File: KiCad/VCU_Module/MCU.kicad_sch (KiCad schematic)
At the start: 0 parts

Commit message: added peripheral pins with the most functionality based on stm32c092rc datasheet, started placing components and routing traces on pcb
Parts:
- added C13, C15, C16, C17: 100n, Capacitor_SMD:C_0805_2012Metric, symbol Device:C_Small
- added C14: 1u, Capacitor_SMD:C_0805_2012Metric, symbol Device:C_Small
- added CR2: ESDCAN03-2BWY, VMS_Footprints:SOT323-3L_STM, symbol ESDCAN03-2BWY:ESDCAN03-2BWY
- added D3: LED, LED_SMD:LED_0805_2012Metric_Pad1.15x1.40mm_HandSolder, symbol Device:LED
- added IC1: STM32C092RCT6, VMS_Footprints:QFP50P1200X1200X160-64N, symbol STM32C092RCT6:STM32C092RCT6
- added J11: Conn_ST_STDC14, Connector_PinHeader_1.27mm:PinHeader_2x07_P1.27mm_Vertical, symbol Connector:Conn_ST_STDC14
- added R24, R25: 10k, Resistor_SMD:R_0805_2012Metric, symbol Device:R_Small_US
- added R26: 120, Resistor_SMD:R_0805_2012Metric, symbol Device:R_Small_US
- added R27, R28: 1k, Resistor_SMD:R_0805_2012Metric, symbol Device:R_Small_US
- added SW2: SW_Push, Button_Switch_THT:SW_PUSH_6mm_H4.3mm, symbol Switch:SW_Push
- added TP12, TP13, TP14, TP15, TP16: TestPoint_Small, TestPoint:TestPoint_THTPad_D1.5mm_Drill0.7mm, symbol Connector:TestPoint_Square
- added U6: MCP2562FDT-H_SN, VMS_Footprints:SOIC127P600X175-8N, symbol MCP2562FDT-H_SN:MCP2562FDT-H_SN
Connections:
- new net: C13.2, IC1.12 (PF2-NRST), J11.12 (~{RST}), R24.2, SW2.1
- new net: D3.2 (A), R27.2
- new net: IC1.30 (PB10), R27.1, R28.1
- new net: IC1.19 (PA2), J11.13 (VCP_RX)
- new net: IC1.20 (PA3), J11.14 (VCP_TX)
- new net: IC1.45 (PA13), J11.4 (JTMS/SWDIO)
- new net: IC1.46 (PA14-BOOT0), J11.6 (JCLK/SWCLK)
- new net +3V3: C14.1, C15.1, C17.1, IC1.7 (VREF+), IC1.8 (VDD/VDDA), J11.3 (VCC), R24.1, U6.5 (VIO)
- new net +5V: C16.2, U6.3 (VDD)
- new net ADC0: IC1.17 (PA0)
- new net ADC1: IC1.18 (PA1)
- new net ADC4: IC1.21 (PA4)
- new net ADC8: IC1.36 (PA8)
- new net CANH: CR2.1, R26.2, TP16.1, U6.7 (CANH)
- new net CANL: CR2.2, R26.1, TP15.1, U6.6 (CANL)
- new net CAN_RXD: IC1.50 (PD0), TP13.1, U6.4 (RXD)
- new net CAN_TXD: IC1.51 (PD1), TP12.1, U6.1 (TXD)
- new net FAULT_LED: R28.2
- new net GND: C13.1, C14.2, C15.2, C16.1, C17.2, CR2.3, D3.1 (K), IC1.9 (VSS/VSSA), J11.11 (GNDDetect), J11.5 (GND), J11.7 (GND), R25.2, SW2.2, U6.2 (VSS)
- new net GPIO_SPARE1_PB6: IC1.60 (PB6)
- new net GPIO_SPARE2_PB7: IC1.61 (PB7)
- new net GPIO_SPARE3_PB8: IC1.62 (PB8)
- new net GPIO_SPARE4_PB9: IC1.63 (PB9)
- new net I2C1_SCL: IC1.37 (PA9)
- new net I2C1_SDA: IC1.42 (PA10)
- new net PB3: IC1.57 (PB3), J11.8 (JTDO/SWO)
- new net SPI1_MISO: IC1.23 (PA6)
- new net SPI1_MOSI: IC1.24 (PA7)
- new net SPI1_NSS: IC1.47 (PA15)
- new net SPI1_SCK: IC1.22 (PA5)
- new net STDBY: IC1.52 (PD2), R25.1, TP14.1, U6.8 (STBY)
- new net TIM1_CH1: IC1.48 (PC8)
- new net TIM1_CH2: IC1.49 (PC9)
- new net TIM1_CH4: IC1.1 (PC11)
- new net TIM1_ETR/BKIN: IC1.3 (PC13)
- new net TIM2_CH1: IC1.25 (PC4)
- new net TIM2_CH2: IC1.26 (PC5)
- no-connect marks 0 -> 29
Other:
- note added: "CAN_STBY: MCU output; HIGH = CAN standby, LOW = normal mode"
- note added: "MCU PIN ASSIGNMENT / INTERFACE SUMMARY Function MCU Pin Net Name Direction / Notes --------------------------------------------------------------- SWDIO PA13 SWDIO STDC14 debug / programming SWCLK PA14 SWCLK STDC14 debug / programming NRST PF2 NRST Hardware reset; connected to reset button and STDC14 RST CAN RX PD0 CAN_RX MCU receives from CAN transceiver RXD CAN TX PD1 CAN_TX MCU transmits to CA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"
- note added: "Populate only if BMU is end node"
- company: (none) -> VIKING MOTOR SPORTS (VMS)
- title: (none) -> VEHICLE CONTROL UNIT (VCU) MODULE

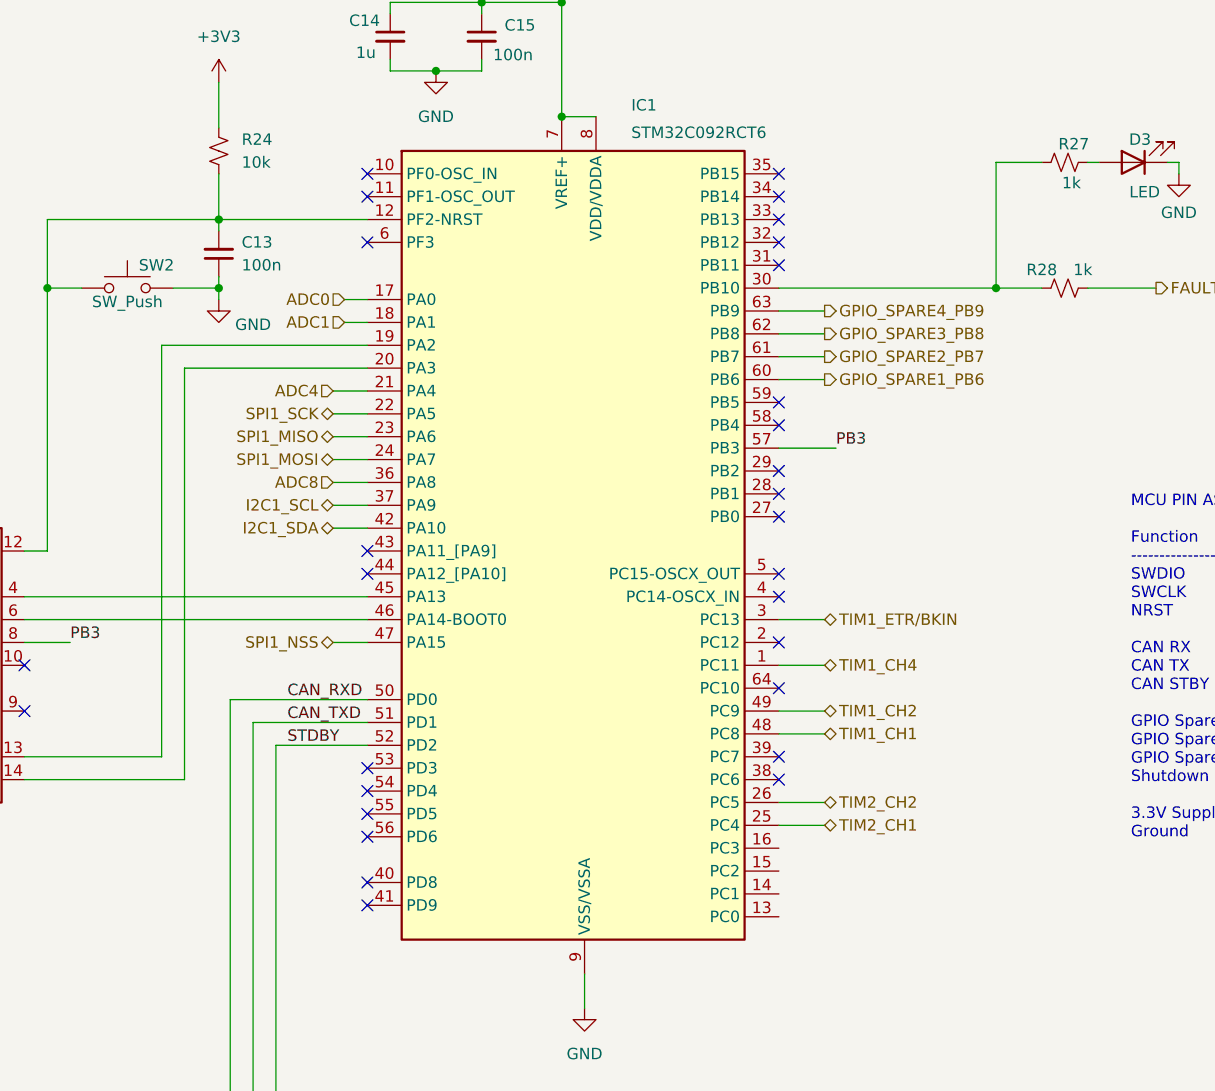
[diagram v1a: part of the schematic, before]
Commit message: adding 'devkit' headers to make connections sustomizable inside of the enclosure
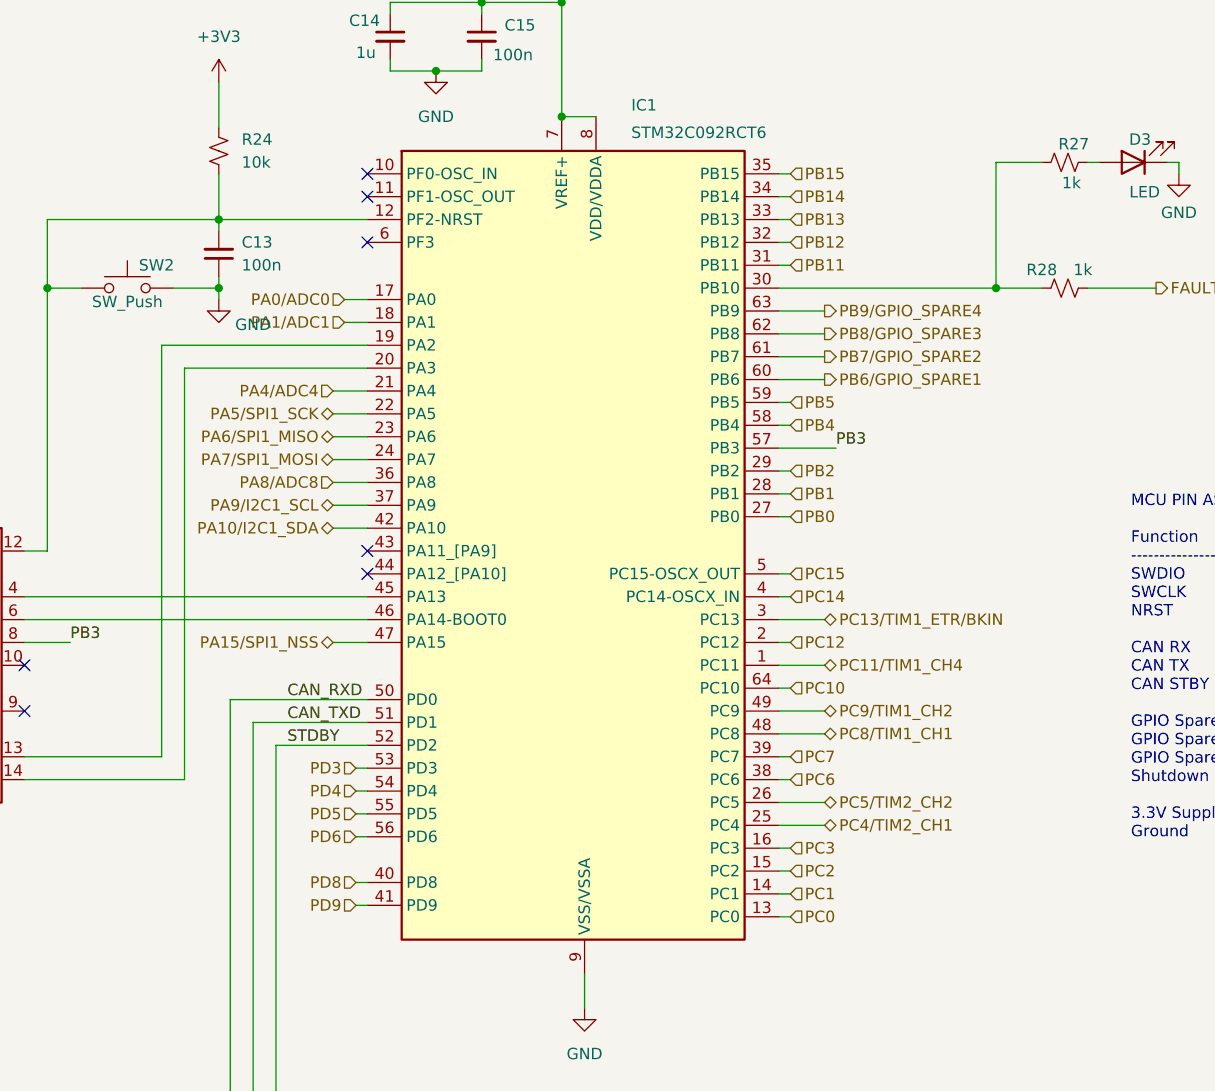
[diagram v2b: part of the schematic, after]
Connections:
- net PC0: now reaches IC1.13 (PC0)
- net PC1: now reaches IC1.14 (PC1)
- net PC2: now reaches IC1.15 (PC2)
- net PC3: now reaches IC1.16 (PC3)
- net PC12: now reaches IC1.2 (PC12)
- net PB0: now reaches IC1.27 (PB0)
- net PB1: now reaches IC1.28 (PB1)
- net PB2: now reaches IC1.29 (PB2)
- net PB11: now reaches IC1.31 (PB11)
- net PB12: now reaches IC1.32 (PB12)
- net PB13: now reaches IC1.33 (PB13)
- net PB14: now reaches IC1.34 (PB14)
- net PB15: now reaches IC1.35 (PB15)
- net PC6: now reaches IC1.38 (PC6)
- net PC7: now reaches IC1.39 (PC7)
- net PC14: now reaches IC1.4 (PC14-OSCX_IN)
- net PD8: now reaches IC1.40 (PD8)
- net PD9: now reaches IC1.41 (PD9)
- net PC15: now reaches IC1.5 (PC15-OSCX_OUT)
- net PD3: now reaches IC1.53 (PD3)
- net PD4: now reaches IC1.54 (PD4)
- net PD5: now reaches IC1.55 (PD5)
- net PD6: now reaches IC1.56 (PD6)
- net PB4: now reaches IC1.58 (PB4)
- net PB5: now reaches IC1.59 (PB5)
- net PC10: now reaches IC1.64 (PC10)
- net ADC0 renamed PA0/ADC0
- net ADC1 renamed PA1/ADC1
- net ADC4 renamed PA4/ADC4
- net ADC8 renamed PA8/ADC8
- net GPIO_SPARE1_PB6 renamed PB6/GPIO_SPARE1
- net GPIO_SPARE2_PB7 renamed PB7/GPIO_SPARE2
- net GPIO_SPARE3_PB8 renamed PB8/GPIO_SPARE3
- net GPIO_SPARE4_PB9 renamed PB9/GPIO_SPARE4
- net I2C1_SCL renamed PA9/I2C1_SCL
- net I2C1_SDA renamed PA10/I2C1_SDA
- net SPI1_MISO renamed PA6/SPI1_MISO
- net SPI1_MOSI renamed PA7/SPI1_MOSI
- net SPI1_NSS renamed PA15/SPI1_NSS
- net SPI1_SCK renamed PA5/SPI1_SCK
- net TIM1_CH1 renamed PC8/TIM1_CH1
- net TIM1_CH2 renamed PC9/TIM1_CH2
- net TIM1_CH4 renamed PC11/TIM1_CH4
- net TIM1_ETR/BKIN renamed PC13/TIM1_ETR/BKIN
- net TIM2_CH1 renamed PC4/TIM2_CH1
- net TIM2_CH2 renamed PC5/TIM2_CH2
- no-connect marks 29 -> 7

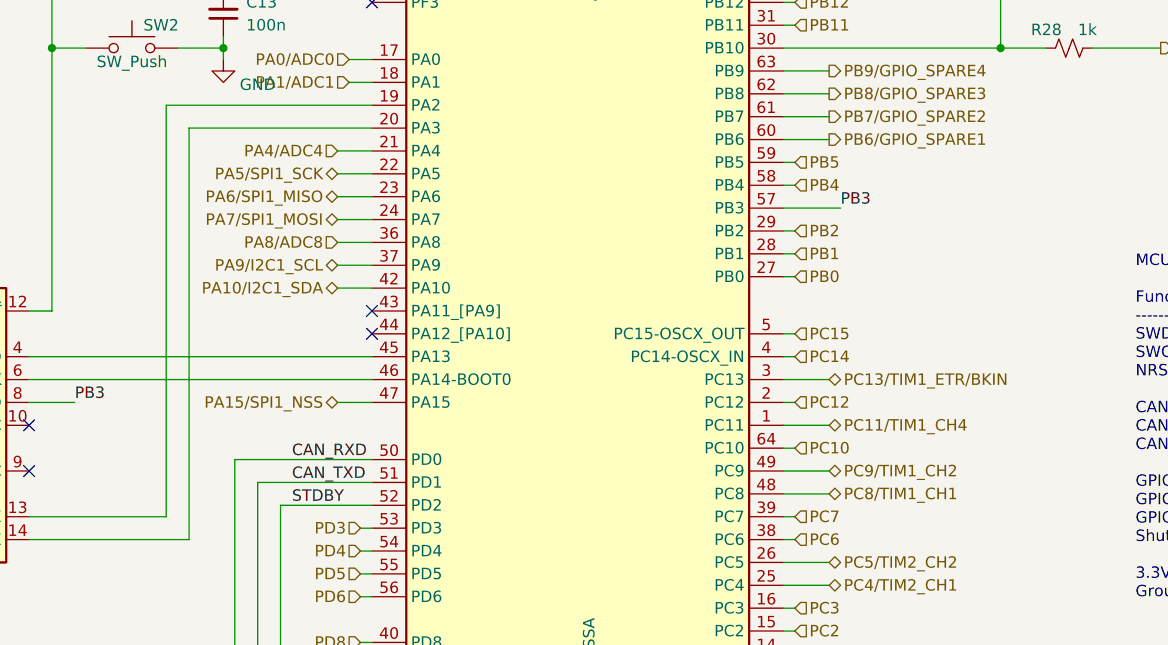
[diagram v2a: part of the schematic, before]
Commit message: added new power supply components, new power supply circuitry needs finishing
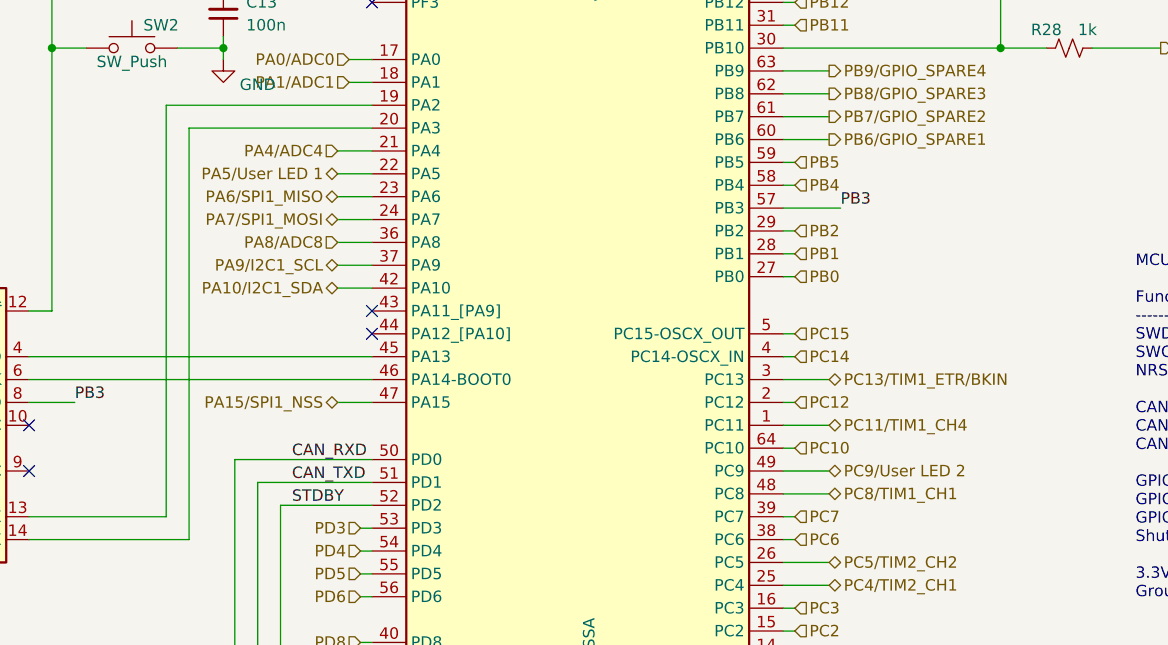
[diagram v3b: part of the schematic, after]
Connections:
- net PA5/SPI1_SCK renamed PA5/User LED 1
- net PC9/TIM1_CH2 renamed PC9/User LED 2
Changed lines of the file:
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@@
 		)
 	)
-	(hierarchical_label "PC9{slash}TIM1_CH2"
+	(hierarchical_label "PC9{slash}User LED 2"
 		(shape bidirectional)
 		(at 212.09 128.27 0)
@@
 		)
 	)
-	(hierarchical_label "PA5{slash}SPI1_SCK"
+	(hierarchical_label "PA5{slash}User LED 1"
 		(shape bidirectional)
 		(at 157.48 95.25 180)

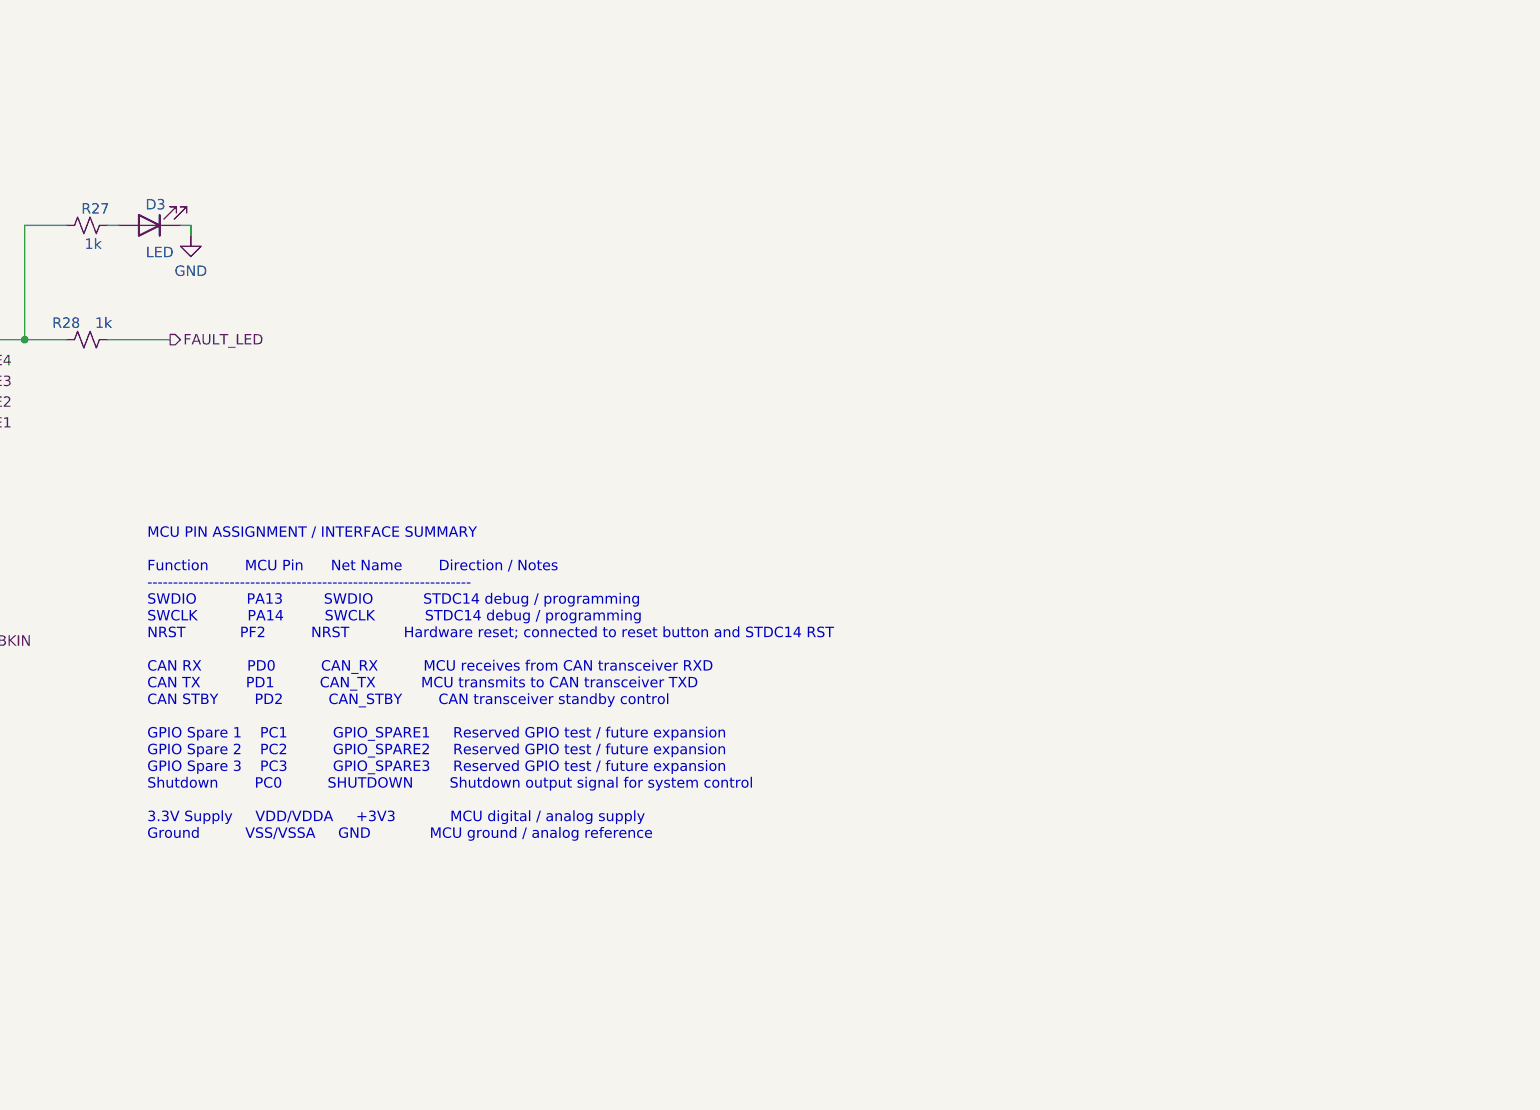
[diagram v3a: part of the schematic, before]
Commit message: finished reworking power supply with new LMR regulators, reorganized schematic, added description to top page, added user leds with identical layout to the nucleo c092 schematic
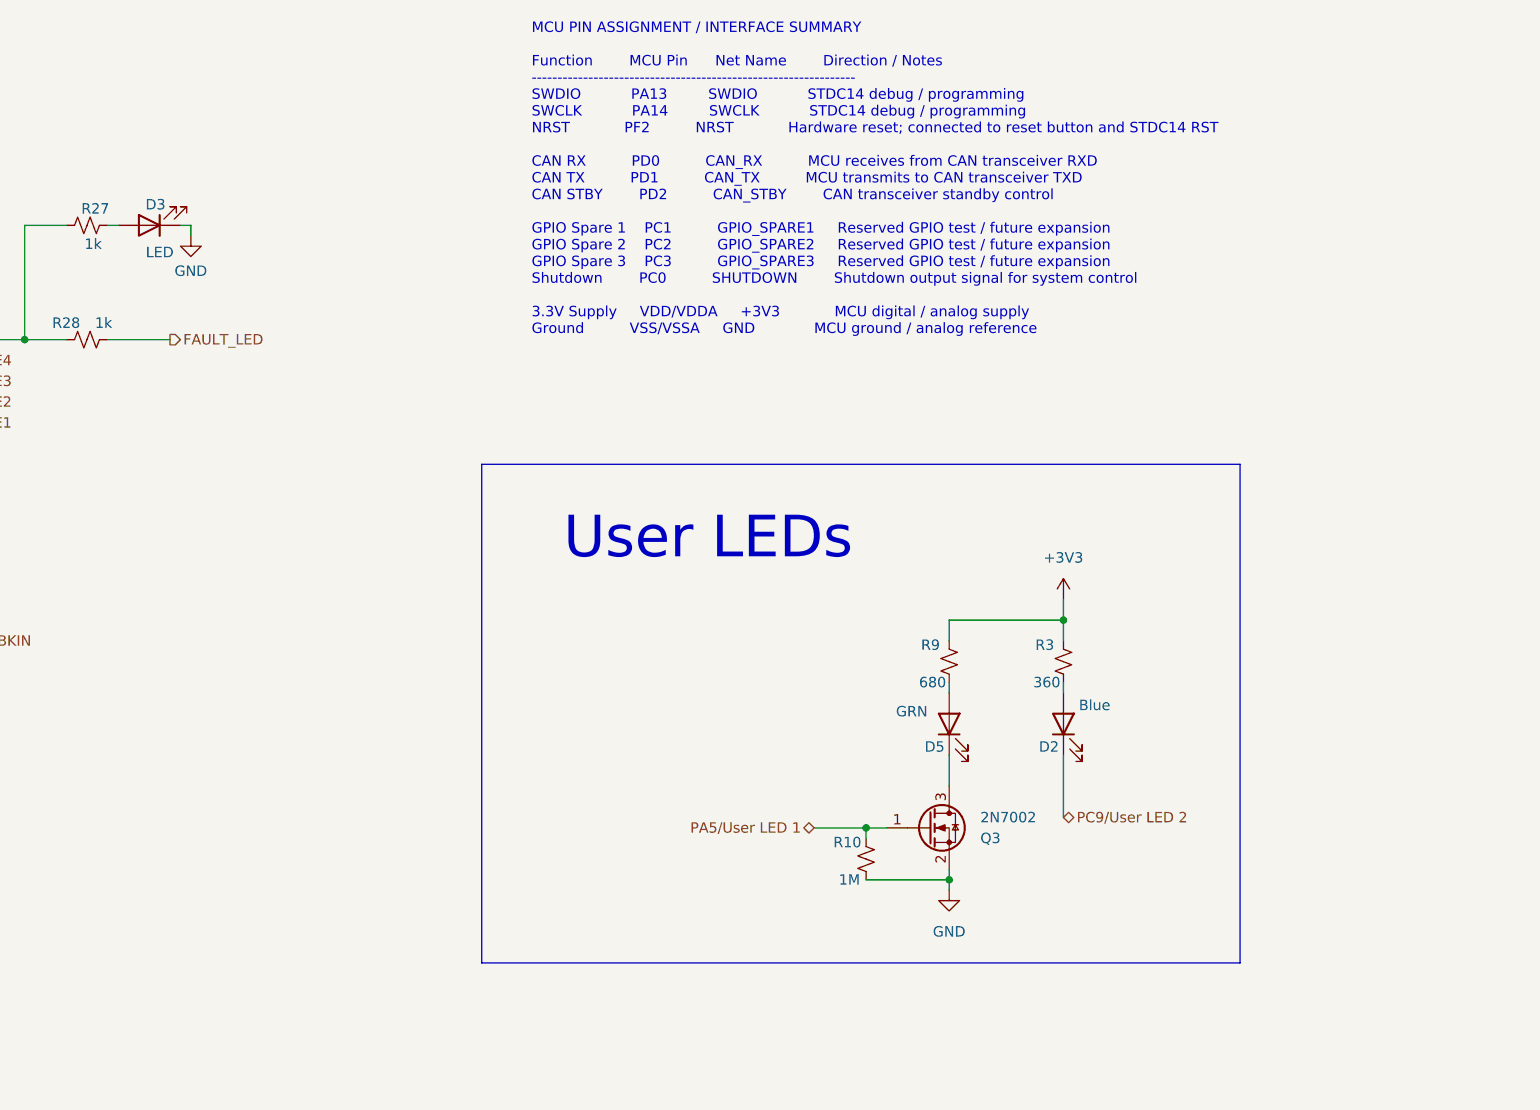
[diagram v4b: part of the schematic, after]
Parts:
- added D2: Blue, LED_SMD:LED_0805_2012Metric_Pad1.15x1.40mm_HandSolder, symbol Device:LED
- added D5: GRN, LED_SMD:LED_0805_2012Metric_Pad1.15x1.40mm_HandSolder, symbol Device:LED
- added Q3: 2N7002, Package_TO_SOT_SMD:SOT-23, symbol Transistor_FET:2N7002
- added R10: 1M, Resistor_SMD:R_0805_2012Metric, symbol Device:R_Small_US
- added R3: 360, Resistor_SMD:R_0805_2012Metric, symbol Device:R_Small_US
- added R9: 680, Resistor_SMD:R_0805_2012Metric, symbol Device:R_Small_US
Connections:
- net +3V3: now also R3.2, R9.2
- net GND: now also Q3.2 (S), R10.1
- net PA5/User LED 1: now also Q3.1 (G), R10.2
- net PC9/User LED 2: now also D2.1 (K)
- new net: D2.2 (A), R3.1
- new net: D5.2 (A), R9.1
- new net: D5.1 (K), Q3.3 (D)
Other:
- note added: "User LEDs"
- title: VEHICLE CONTROL UNIT (VCU) MODULE -> VEHICLE CONTROL UNIT (VCU) Dev Board
